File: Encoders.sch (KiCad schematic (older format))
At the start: 32 parts

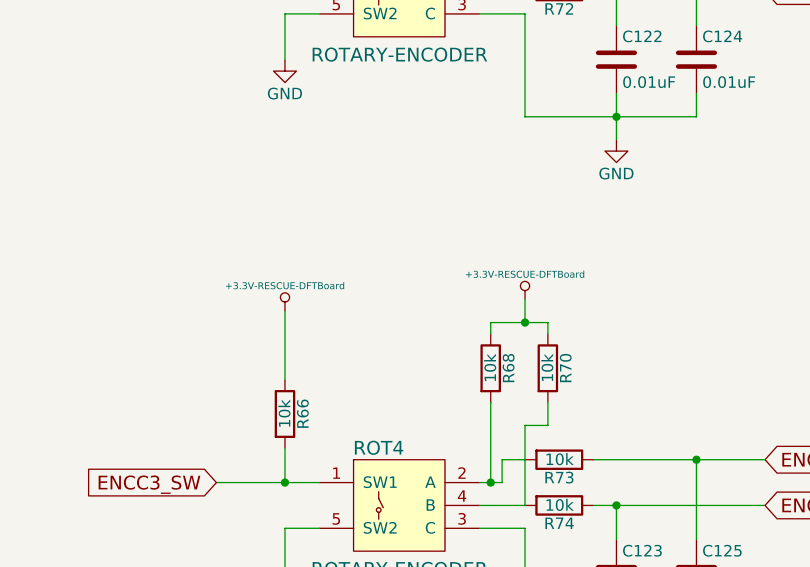
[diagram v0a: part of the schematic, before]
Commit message: resolved ERC errors, and began assigning footprints
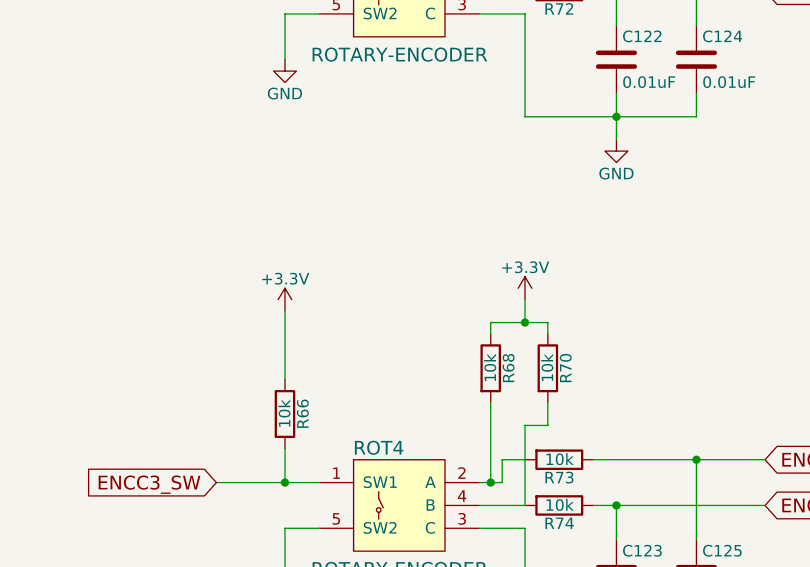
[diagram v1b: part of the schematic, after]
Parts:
- C118, C119, C120, C121, C122, C123, C124, C125: footprint (none) -> Capacitors_SMD:C_0402
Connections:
- net +3.3V renamed +3V3

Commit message: added resistor footprints (1206)
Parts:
- R55, R56, R57, R58, R59, R60, R61, R62, R63, R64, R65, R66, R67, R68, R69, R70, R71, R72, R73, R74: footprint (none) -> Resistors_SMD:R_1206
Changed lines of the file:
@@
 F 0 "R62" V 4230 2600 50  0000 C CNN
 F 1 "10k" V 4150 2600 50  0000 C CNN
-F 2 "" V 4080 2600 50  0001 C CNN
+F 2 "Resistors_SMD:R_1206" V 4080 2600 50  0001 C CNN
 F 3 "" H 4150 2600 50  0000 C CNN
 	1    4150 2600
@@
 F 0 "R61" V 4230 2400 50  0000 C CNN
 F 1 "10k" V 4150 2400 50  0000 C CNN
-F 2 "" V 4080 2400 50  0001 C CNN
+F 2 "Resistors_SMD:R_1206" V 4080 2400 50  0001 C CNN
 F 3 "" H 4150 2400 50  0000 C CNN
 	1    4150 2400
@@
 F 0 "R57" V 3930 2000 50  0000 C CNN
 F 1 "10k" V 3850 2000 50  0000 C CNN
-F 2 "" V 3780 2000 50  0001 C CNN
+F 2 "Resistors_SMD:R_1206" V 3780 2000 50  0001 C CNN
 F 3 "" H 3850 2000 50  0000 C CNN
 	1    3850 2000
@@
 F 0 "R59" V 4180 2000 50  0000 C CNN
 F 1 "10k" V 4100 2000 50  0000 C CNN
-F 2 "" V 4030 2000 50  0001 C CNN
+F 2 "Resistors_SMD:R_1206" V 4030 2000 50  0001 C CNN
 F 3 "" H 4100 2000 50  0000 C CNN
 	1    4100 2000
@@
 F 0 "R55" V 3030 2200 50  0000 C CNN
 F 1 "10k" V 2950 2200 50  0000 C CNN
-F 2 "" V 2880 2200 50  0001 C CNN
+F 2 "Resistors_SMD:R_1206" V 2880 2200 50  0001 C CNN
 F 3 "" H 2950 2200 50  0000 C CNN
 	1    2950 2200
@@
 F 0 "R72" V 8530 2600 50  0000 C CNN
 F 1 "10k" V 8450 2600 50  0000 C CNN
-F 2 "" V 8380 2600 50  0001 C CNN
+F 2 "Resistors_SMD:R_1206" V 8380 2600 50  0001 C CNN
 F 3 "" H 8450 2600 50  0000 C CNN
 	1    8450 2600
@@
 F 0 "R71" V 8530 2400 50  0000 C CNN
 F 1 "10k" V 8450 2400 50  0000 C CNN
-F 2 "" V 8380 2400 50  0001 C CNN
+F 2 "Resistors_SMD:R_1206" V 8380 2400 50  0001 C CNN
 F 3 "" H 8450 2400 50  0000 C CNN
 	1    8450 2400
@@
 F 0 "R67" V 8230 2000 50  0000 C CNN
 F 1 "10k" V 8150 2000 50  0000 C CNN
-F 2 "" V 8080 2000 50  0001 C CNN
+F 2 "Resistors_SMD:R_1206" V 8080 2000 50  0001 C CNN
 F 3 "" H 8150 2000 50  0000 C CNN
 	1    8150 2000
@@
 F 0 "R69" V 8480 2000 50  0000 C CNN
 F 1 "10k" V 8400 2000 50  0000 C CNN
-F 2 "" V 8330 2000 50  0001 C CNN
+F 2 "Resistors_SMD:R_1206" V 8330 2000 50  0001 C CNN
 F 3 "" H 8400 2000 50  0000 C CNN
 	1    8400 2000
@@
 F 0 "R65" V 7330 2200 50  0000 C CNN
 F 1 "10k" V 7250 2200 50  0000 C CNN
-F 2 "" V 7180 2200 50  0001 C CNN
+F 2 "Resistors_SMD:R_1206" V 7180 2200 50  0001 C CNN
 F 3 "" H 7250 2200 50  0000 C CNN
 	1    7250 2200
@@
 F 0 "R64" V 4230 4850 50  0000 C CNN
 F 1 "10k" V 4150 4850 50  0000 C CNN
-F 2 "" V 4080 4850 50  0001 C CNN
+F 2 "Resistors_SMD:R_1206" V 4080 4850 50  0001 C CNN
 F 3 "" H 4150 4850 50  0000 C CNN
 	1    4150 4850
@@
 F 0 "R63" V 4230 4650 50  0000 C CNN
 F 1 "10k" V 4150 4650 50  0000 C CNN
-F 2 "" V 4080 4650 50  0001 C CNN
+F 2 "Resistors_SMD:R_1206" V 4080 4650 50  0001 C CNN
 F 3 "" H 4150 4650 50  0000 C CNN
 	1    4150 4650
@@
 F 0 "R58" V 3930 4250 50  0000 C CNN
 F 1 "10k" V 3850 4250 50  0000 C CNN
-F 2 "" V 3780 4250 50  0001 C CNN
+F 2 "Resistors_SMD:R_1206" V 3780 4250 50  0001 C CNN
 F 3 "" H 3850 4250 50  0000 C CNN
 	1    3850 4250
@@
 F 0 "R60" V 4180 4250 50  0000 C CNN
 F 1 "10k" V 4100 4250 50  0000 C CNN
-F 2 "" V 4030 4250 50  0001 C CNN
+F 2 "Resistors_SMD:R_1206" V 4030 4250 50  0001 C CNN
 F 3 "" H 4100 4250 50  0000 C CNN
 	1    4100 4250
@@
 F 0 "R56" V 3030 4450 50  0000 C CNN
 F 1 "10k" V 2950 4450 50  0000 C CNN
-F 2 "" V 2880 4450 50  0001 C CNN
+F 2 "Resistors_SMD:R_1206" V 2880 4450 50  0001 C CNN
 F 3 "" H 2950 4450 50  0000 C CNN
 	1    2950 4450
@@
 F 0 "R74" V 8530 4850 50  0000 C CNN
 F 1 "10k" V 8450 4850 50  0000 C CNN
-F 2 "" V 8380 4850 50  0001 C CNN
+F 2 "Resistors_SMD:R_1206" V 8380 4850 50  0001 C CNN
 F 3 "" H 8450 4850 50  0000 C CNN
 	1    8450 4850
@@
 F 0 "R73" V 8530 4650 50  0000 C CNN
 F 1 "10k" V 8450 4650 50  0000 C CNN
-F 2 "" V 8380 4650 50  0001 C CNN
+F 2 "Resistors_SMD:R_1206" V 8380 4650 50  0001 C CNN
 F 3 "" H 8450 4650 50  0000 C CNN
 	1    8450 4650
@@
 F 0 "R68" V 8230 4250 50  0000 C CNN
 F 1 "10k" V 8150 4250 50  0000 C CNN
-F 2 "" V 8080 4250 50  0001 C CNN
+F 2 "Resistors_SMD:R_1206" V 8080 4250 50  0001 C CNN
 F 3 "" H 8150 4250 50  0000 C CNN
 	1    8150 4250
@@
 F 0 "R70" V 8480 4250 50  0000 C CNN
 F 1 "10k" V 8400 4250 50  0000 C CNN
-F 2 "" V 8330 4250 50  0001 C CNN
+F 2 "Resistors_SMD:R_1206" V 8330 4250 50  0001 C CNN
 F 3 "" H 8400 4250 50  0000 C CNN
 	1    8400 4250
@@
 F 0 "R66" V 7330 4450 50  0000 C CNN
 F 1 "10k" V 7250 4450 50  0000 C CNN
-F 2 "" V 7180 4450 50  0001 C CNN
+F 2 "Resistors_SMD:R_1206" V 7180 4450 50  0001 C CNN
 F 3 "" H 7250 4450 50  0000 C CNN
 	1    7250 4450

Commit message: ???
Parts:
- ROT1, ROT2, ROT3, ROT4: footprint (none) -> encoder:rightangle encoders
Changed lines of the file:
@@
 F 0 "ROT1" H 3360 2850 60  0000 C CNN
 F 1 "ROTARY-ENCODER" H 3450 2320 60  0000 C CNN
-F 2 "" H 3450 2600 60  0001 C CNN
+F 2 "encoder:rightangle encoders" H 3450 2600 60  0001 C CNN
 F 3 "" H 3450 2600 60  0000 C CNN
 	1    3450 2600
@@
 Connection ~ 4000 1800
 $Comp
-L +1.8V #PWR134
+L +1.8V #PWR0131
 U 1 1 586C41F4
 P 4000 1700
-F 0 "#PWR134" H 4000 1840 20  0001 C CNN
+F 0 "#PWR0131" H 4000 1840 20  0001 C CNN
 F 1 "+1.8V" H 4000 1810 30  0000 C CNN
 F 2 "" H 4000 1700 60  0001 C CNN
@@
 $EndComp
 $Comp
-L GND #PWR136
+L GND #PWR0132
 U 1 1 586C4216
 P 4400 3250
-F 0 "#PWR136" H 4400 3000 50  0001 C CNN
+F 0 "#PWR0132" H 4400 3000 50  0001 C CNN
 F 1 "GND" H 4400 3100 50  0000 C CNN
 F 2 "" H 4400 3250 50  0000 C CNN
@@
 	2950 2700 2950 2900
 $Comp
-L GND #PWR131
+L GND #PWR0133
 U 1 1 586C437C
 P 2950 2900
-F 0 "#PWR131" H 2950 2650 50  0001 C CNN
+F 0 "#PWR0133" H 2950 2650 50  0001 C CNN
 F 1 "GND" H 2950 2750 50  0000 C CNN
 F 2 "" H 2950 2900 50  0000 C CNN
@@
 $EndComp
 $Comp
-L +1.8V #PWR130
+L +1.8V #PWR0134
 U 1 1 586C43A0
 P 2950 1750
-F 0 "#PWR130" H 2950 1890 20  0001 C CNN
+F 0 "#PWR0134" H 2950 1890 20  0001 C CNN
 F 1 "+1.8V" H 2950 1860 30  0000 C CNN
 F 2 "" H 2950 1750 60  0001 C CNN
@@
 F 0 "ROT3" H 7660 2850 60  0000 C CNN
 F 1 "ROTARY-ENCODER" H 7750 2320 60  0000 C CNN
-F 2 "" H 7750 2600 60  0001 C CNN
+F 2 "encoder:rightangle encoders" H 7750 2600 60  0001 C CNN
 F 3 "" H 7750 2600 60  0000 C CNN
 	1    7750 2600
@@
 Connection ~ 8300 1800
 $Comp
-L +1.8V #PWR142
+L +1.8V #PWR0135
 U 1 1 586C5734
 P 8300 1700
-F 0 "#PWR142" H 8300 1840 20  0001 C CNN
+F 0 "#PWR0135" H 8300 1840 20  0001 C CNN
 F 1 "+1.8V" H 8300 1810 30  0000 C CNN
 F 2 "" H 8300 1700 60  0001 C CNN
@@
 $EndComp
 $Comp
-L GND #PWR144
+L GND #PWR0136
 U 1 1 586C573A
 P 8700 3250
-F 0 "#PWR144" H 8700 3000 50  0001 C CNN
+F 0 "#PWR0136" H 8700 3000 50  0001 C CNN
 F 1 "GND" H 8700 3100 50  0000 C CNN
 F 2 "" H 8700 3250 50  0000 C CNN
@@
 	7250 2700 7250 2900
 $Comp
-L GND #PWR139
+L GND #PWR0137
 U 1 1 586C5748
 P 7250 2900
-F 0 "#PWR139" H 7250 2650 50  0001 C CNN
+F 0 "#PWR0137" H 7250 2650 50  0001 C CNN
 F 1 "GND" H 7250 2750 50  0000 C CNN
 F 2 "" H 7250 2900 50  0000 C CNN
@@
 $EndComp
 $Comp
-L +1.8V #PWR138
+L +1.8V #PWR0138
 U 1 1 586C574E
 P 7250 1750
-F 0 "#PWR138" H 7250 1890 20  0001 C CNN
+F 0 "#PWR0138" H 7250 1890 20  0001 C CNN
 F 1 "+1.8V" H 7250 1860 30  0000 C CNN
 F 2 "" H 7250 1750 60  0001 C CNN
@@
 F 0 "ROT2" H 3360 5100 60  0000 C CNN
 F 1 "ROTARY-ENCODER" H 3450 4570 60  0000 C CNN
-F 2 "" H 3450 4850 60  0001 C CNN
+F 2 "encoder:rightangle encoders" H 3450 4850 60  0001 C CNN
 F 3 "" H 3450 4850 60  0000 C CNN
 	1    3450 4850
@@
 Connection ~ 4000 4050
 $Comp
-L +1.8V #PWR135
+L +1.8V #PWR0139
 U 1 1 586C5B7F
 P 4000 3950
-F 0 "#PWR135" H 4000 4090 20  0001 C CNN
+F 0 "#PWR0139" H 4000 4090 20  0001 C CNN
 F 1 "+1.8V" H 4000 4060 30  0000 C CNN
 F 2 "" H 4000 3950 60  0001 C CNN
@@
 $EndComp
 $Comp
-L GND #PWR137
+L GND #PWR0140
 U 1 1 586C5B85
 P 4400 5500
-F 0 "#PWR137" H 4400 5250 50  0001 C CNN
+F 0 "#PWR0140" H 4400 5250 50  0001 C CNN
 F 1 "GND" H 4400 5350 50  0000 C CNN
 F 2 "" H 4400 5500 50  0000 C CNN
@@
 	2950 4950 2950 5150
 $Comp
-L GND #PWR133
+L GND #PWR0141
 U 1 1 586C5B93
 P 2950 5150
-F 0 "#PWR133" H 2950 4900 50  0001 C CNN
+F 0 "#PWR0141" H 2950 4900 50  0001 C CNN
 F 1 "GND" H 2950 5000 50  0000 C CNN
 F 2 "" H 2950 5150 50  0000 C CNN
@@
 $EndComp
 $Comp
-L +1.8V #PWR132
+L +1.8V #PWR0142
 U 1 1 586C5B99
 P 2950 4000
-F 0 "#PWR132" H 2950 4140 20  0001 C CNN
+F 0 "#PWR0142" H 2950 4140 20  0001 C CNN
 F 1 "+1.8V" H 2950 4110 30  0000 C CNN
 F 2 "" H 2950 4000 60  0001 C CNN
@@
 F 0 "ROT4" H 7660 5100 60  0000 C CNN
 F 1 "ROTARY-ENCODER" H 7750 4570 60  0000 C CNN
-F 2 "" H 7750 4850 60  0001 C CNN
+F 2 "encoder:rightangle encoders" H 7750 4850 60  0001 C CNN
 F 3 "" H 7750 4850 60  0000 C CNN
 	1    7750 4850
@@
 Connection ~ 8300 4050
 $Comp
-L GND #PWR145
+L GND #PWR0143
 U 1 1 586C62A0
 P 8700 5500
-F 0 "#PWR145" H 8700 5250 50  0001 C CNN
+F 0 "#PWR0143" H 8700 5250 50  0001 C CNN
 F 1 "GND" H 8700 5350 50  0000 C CNN
 F 2 "" H 8700 5500 50  0000 C CNN
@@
 	7250 4950 7250 5150
 $Comp
-L GND #PWR141
+L GND #PWR0144
 U 1 1 586C62AE
 P 7250 5150
-F 0 "#PWR141" H 7250 4900 50  0001 C CNN
+F 0 "#PWR0144" H 7250 4900 50  0001 C CNN
 F 1 "GND" H 7250 5000 50  0000 C CNN
 F 2 "" H 7250 5150 50  0000 C CNN
@@
 Connection ~ 7250 4750
 $Comp
-L +3.3V #PWR143
+L +3.3V #PWR0145
 U 1 1 587428B8
 P 8300 3950
-F 0 "#PWR143" H 8300 3800 50  0001 C CNN
+F 0 "#PWR0145" H 8300 3800 50  0001 C CNN
 F 1 "+3.3V" H 8300 4090 50  0000 C CNN
 F 2 "" H 8300 3950 50  0000 C CNN
@@
 $EndComp
 $Comp
-L +3.3V #PWR140
+L +3.3V #PWR0146
 U 1 1 58742FBB
 P 7250 4000
-F 0 "#PWR140" H 7250 3850 50  0001 C CNN
+F 0 "#PWR0146" H 7250 3850 50  0001 C CNN
 F 1 "+3.3V" H 7250 4140 50  0000 C CNN
 F 2 "" H 7250 4000 50  0000 C CNN

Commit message: fixed a few diagram/footprint pin mismatches, getting ready to pull gene's microhdmi footprint
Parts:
- ROT1, ROT2, ROT3, ROT4: footprint encoder:rightangle encoders -> DFTcustom:rightangleencoders
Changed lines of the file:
@@
 LIBS:ferrite
 LIBS:df_device
+LIBS:JACK_TRS_5PINS
 EELAYER 25 0
 EELAYER END
@@
 F 0 "ROT1" H 3360 2850 60  0000 C CNN
 F 1 "ROTARY-ENCODER" H 3450 2320 60  0000 C CNN
-F 2 "encoder:rightangle encoders" H 3450 2600 60  0001 C CNN
+F 2 "DFTcustom:rightangleencoders" H 3450 2600 60  0001 C CNN
 F 3 "" H 3450 2600 60  0000 C CNN
 	1    3450 2600
@@
 F 0 "ROT3" H 7660 2850 60  0000 C CNN
 F 1 "ROTARY-ENCODER" H 7750 2320 60  0000 C CNN
-F 2 "encoder:rightangle encoders" H 7750 2600 60  0001 C CNN
+F 2 "DFTcustom:rightangleencoders" H 7750 2600 60  0001 C CNN
 F 3 "" H 7750 2600 60  0000 C CNN
 	1    7750 2600
@@
 F 0 "ROT2" H 3360 5100 60  0000 C CNN
 F 1 "ROTARY-ENCODER" H 3450 4570 60  0000 C CNN
-F 2 "encoder:rightangle encoders" H 3450 4850 60  0001 C CNN
+F 2 "DFTcustom:rightangleencoders" H 3450 4850 60  0001 C CNN
 F 3 "" H 3450 4850 60  0000 C CNN
 	1    3450 4850
@@
 F 0 "ROT4" H 7660 5100 60  0000 C CNN
 F 1 "ROTARY-ENCODER" H 7750 4570 60  0000 C CNN
-F 2 "encoder:rightangle encoders" H 7750 4850 60  0001 C CNN
+F 2 "DFTcustom:rightangleencoders" H 7750 4850 60  0001 C CNN
 F 3 "" H 7750 4850 60  0000 C CNN
 	1    7750 4850
